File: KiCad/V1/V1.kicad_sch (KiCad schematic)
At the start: 84 parts, among them Q1 Q_NMOS_GSD, Q2 Q_NMOS_GSD, T1 Transformer_1P_1S, U1 LMG1210RVRR, U2 OPA2677IDDA, U3 OPA2677IDDA, U4 OPA859QDSGRQ1, U5 OPA859QDSGRQ1, U6 OPA859QDSGRQ1

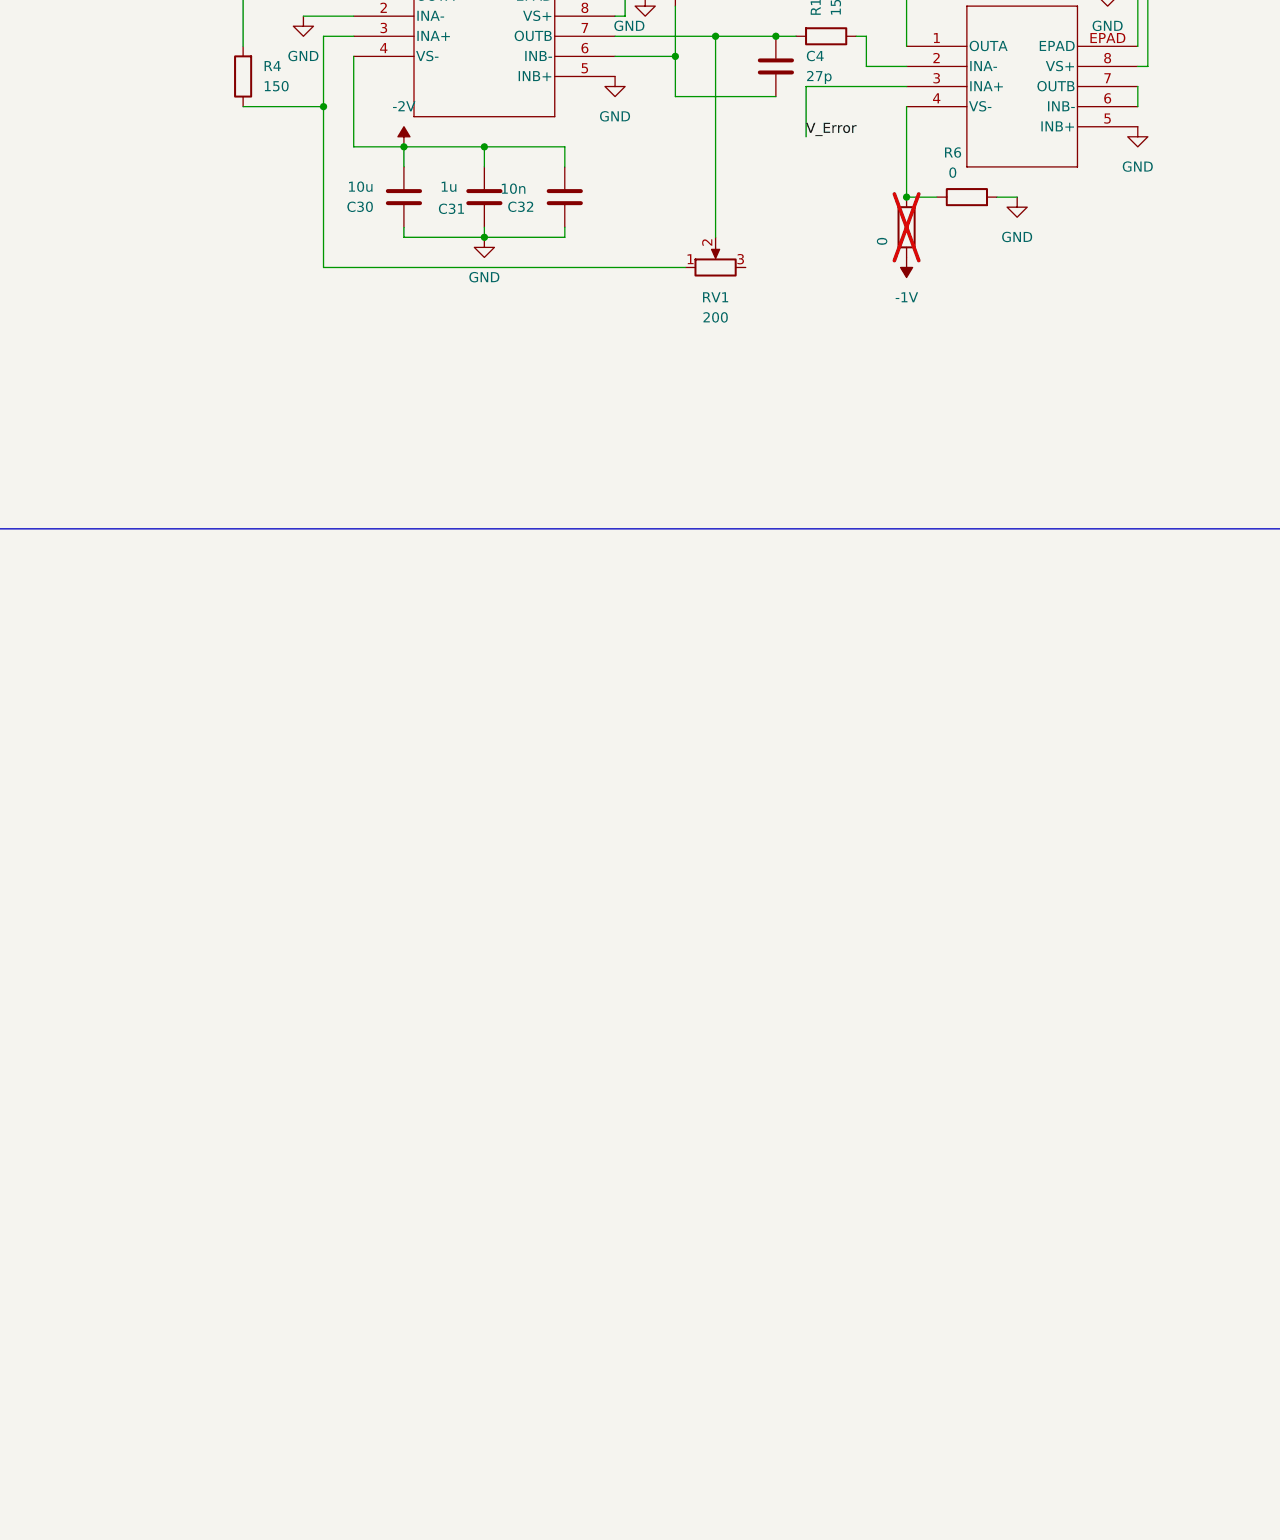
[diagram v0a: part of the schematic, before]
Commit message: fixed pwm gen negative supply voltage
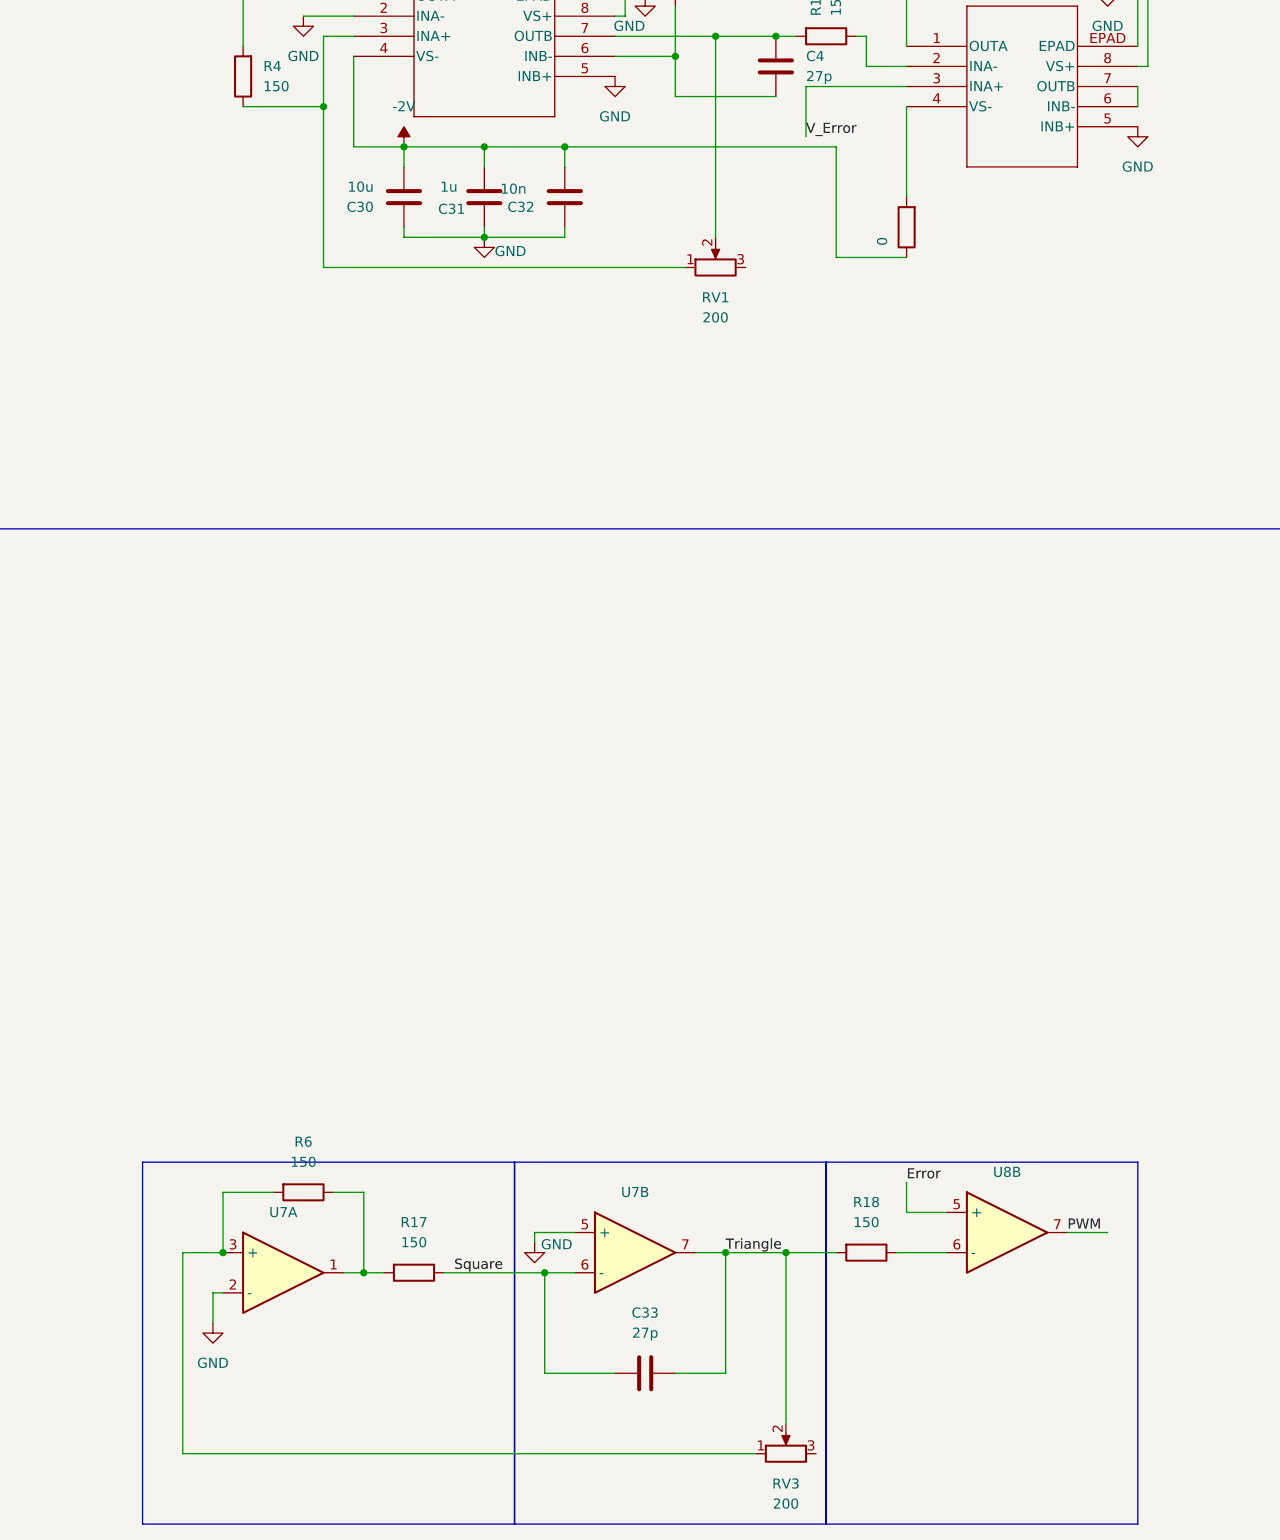
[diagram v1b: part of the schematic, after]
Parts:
- added C33: 27p, Capacitor_SMD:C_0402_1005Metric, symbol Device:C
- added R17, R18: 150, symbol Device:R
- added RV3: 200, MyFootprints:POT_ 3214W-1-201E, symbol Device:R_Potentiometer
- added U7: OPAMP, symbol Device:Opamp_Dual
- added U8: Compariotr, symbol Device:Opamp_Dual
- R3: now fitted
- R6: value 0 -> 150; footprint Capacitor_SMD:C_0805_2012Metric -> (none)
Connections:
- net -1V is gone; now on net -2V: R3.1
- net GND: now also U7.2 (-), U7.5 (+); no longer R6.2
- net at R3.2, U3.4 (VS-): no longer R6.1
- new net: R17.2, R6.1, U7.1
- new net: R6.2, RV3.1, U7.3 (+)
- new net: R18.1, U8.6 (-)
- new net Error: U8.5 (+)
- new net PWM: U8.7
- new net Square: C33.1, R17.1, U7.6 (-)
- new net Triangle: C33.2, R18.2, RV3.2, U7.7

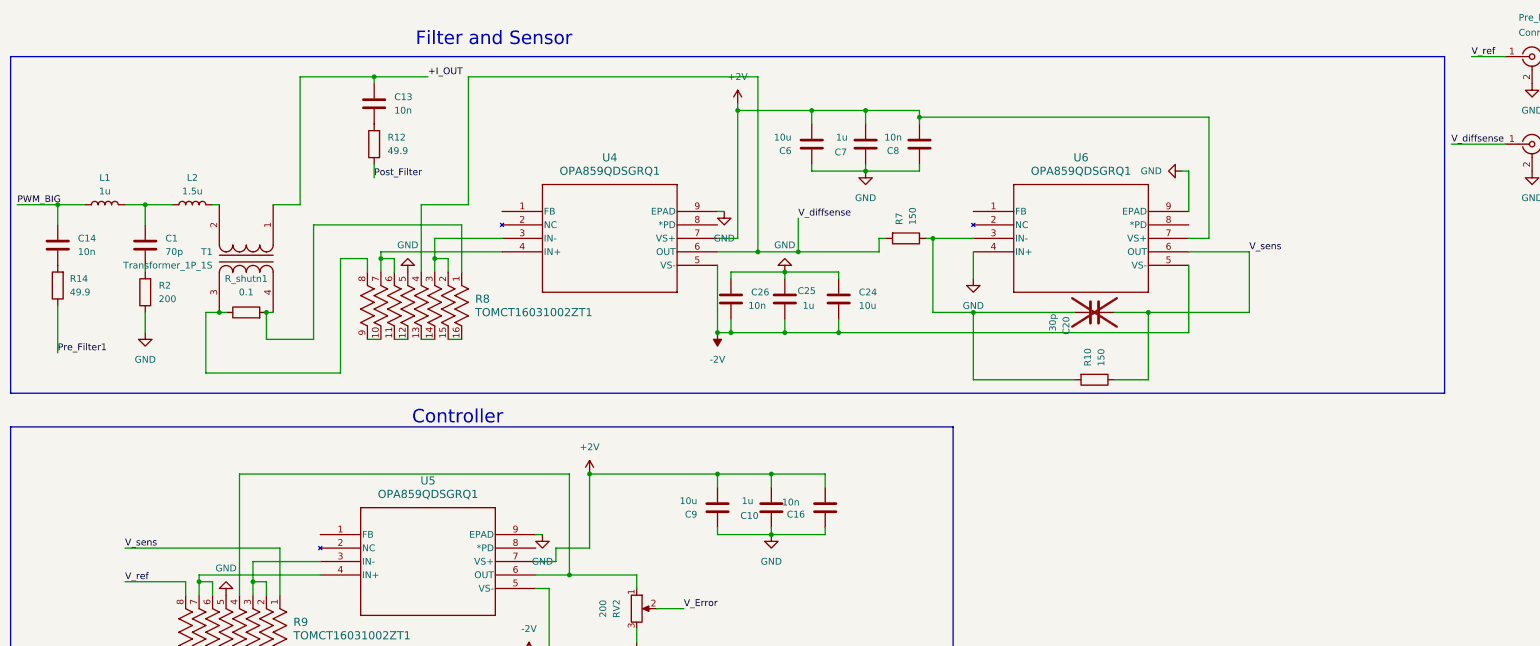
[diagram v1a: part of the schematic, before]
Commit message: aded alternative path for curent sense signal
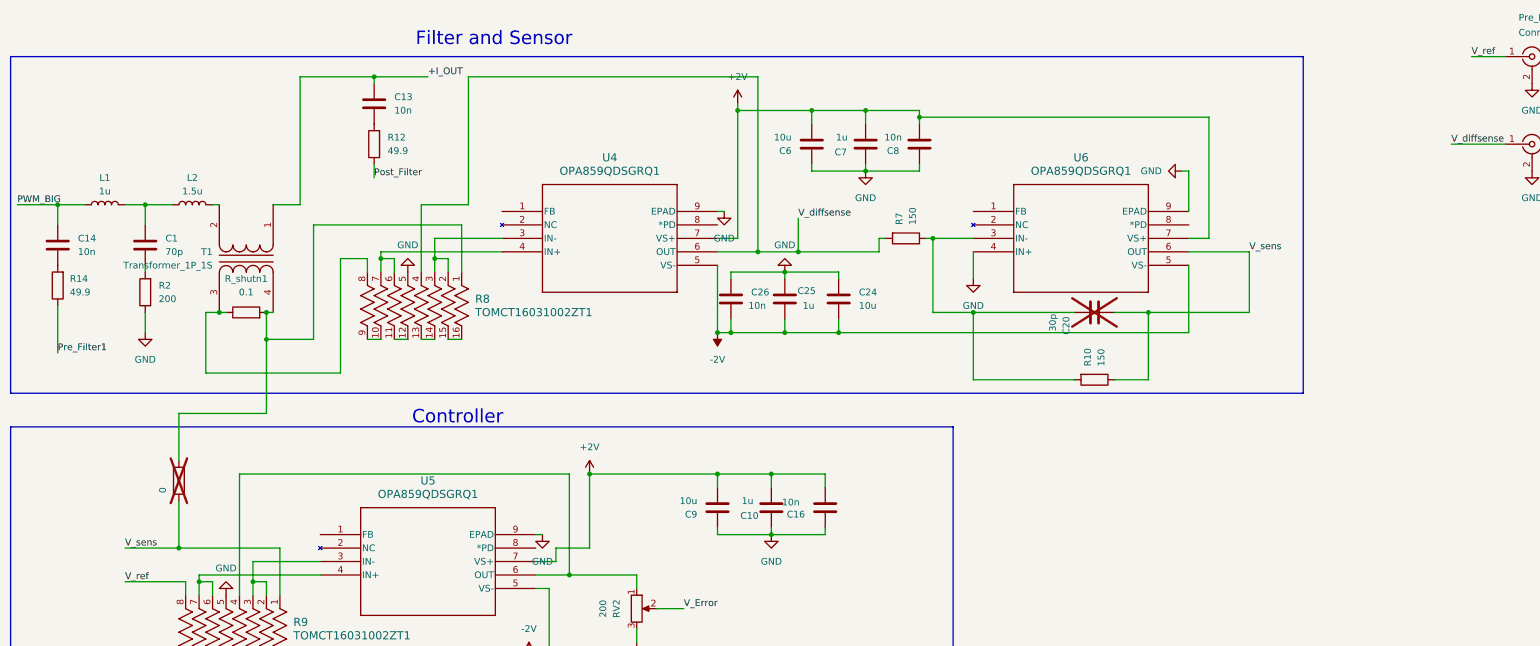
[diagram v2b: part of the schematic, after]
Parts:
- added R19: 0, Capacitor_SMD:C_0805_2012Metric, symbol Device:R
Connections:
- net V_sens: now also R19.1
- net at R8.1, R_shutn1.2, T1.4 (SB): now also R19.2
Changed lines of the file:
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@@
 	)
 	(junction
+		(at 54.61 115.57)
+		(diameter 0)
+		(color 0 0 0 0)
+	)
+	(junction
 		(at 95.25 217.17)
 		(diameter 0)
@@
 	)
 	(junction
+		(at 71.12 76.2)
+		(diameter 0)
+		(color 0 0 0 0)
+	)
+	(junction
 		(at 156.21 74.93)
 		(diameter 0)
@@
 	(wire
 		(pts
-			(xy 44.45 115.57) (xy 73.66 115.57)
+			(xy 44.45 115.57) (xy 54.61 115.57)
 		)
 		(stroke
@@
 	(wire
 		(pts
+			(xy 54.61 90.17) (xy 71.12 90.17)
+		)
+		(stroke
+			(width 0)
+			(type default)
+		)
+	)
+	(wire
+		(pts
 			(xy 74.93 217.17) (xy 85.09 217.17)
 		)
@@
 	(wire
 		(pts
+			(xy 54.61 99.06) (xy 54.61 90.17)
+		)
+		(stroke
+			(width 0)
+			(type default)
+		)
+	)
+	(wire
+		(pts
 			(xy 48.26 71.12) (xy 48.26 74.93)
 		)
@@
 	(wire
 		(pts
+			(xy 71.12 90.17) (xy 71.12 76.2)
+		)
+		(stroke
+			(width 0)
+			(type default)
+		)
+	)
+	(wire
+		(pts
 			(xy 311.15 175.26) (xy 320.04 175.26)
 		)
@@
 	(wire
 		(pts
+			(xy 54.61 106.68) (xy 54.61 115.57)
+		)
+		(stroke
+			(width 0)
+			(type default)
+		)
+	)
+	(wire
+		(pts
 			(xy 138.43 189.23) (xy 140.97 189.23)
 		)
@@
 	(wire
 		(pts
+			(xy 54.61 115.57) (xy 73.66 115.57)
+		)
+		(stroke
+			(width 0)
+			(type default)
+		)
+	)
+	(wire
+		(pts
 			(xy 68.58 191.77) (xy 68.58 198.12)
 		)
@@
 	(rectangle
 		(start 22.86 22.86)
-		(end 293.37 86.36)
+		(end 266.7 86.36)
 		(stroke
 			(width 0)
@@
 					(unit 1)
 				)
+			)
+		)
+	)
+	(symbol
+		(lib_id "Device:R")
+		(at 54.61 102.87 180)
+		(unit 1)
+		(exclude_from_sim no)
+		(in_bom yes)
+		(on_board yes)
+		(dnp yes)
+		(property "Reference" "R19"
+			(at 49.022 104.648 90)
+			(effects
+				(font
+					(size 1.27 1.27)
+				)
+				(hide yes)
+			)
+		)
+		(property "Value" "0"
+			(at 51.562 104.648 90)
+			(effects
+				(font
+					(size 1.27 1.27)
+				)
+			)
+		)
+		(property "Footprint" "Capacitor_SMD:C_0805_2012Metric"
+			(at 56.388 102.87 90)
+			(effects
+				(font
+					(size 1.27 1.27)
+				)
+				(hide yes)
+			)
+		)
+		(property "Datasheet" "~"
+			(at 54.61 102.87 0)
+			(effects
+				(font
+					(size 1.27 1.27)
+				)
+				(hide yes)
+			)
+		)
+		(property "Description" "Resistor"
+			(at 54.61 102.87 0)
+			(effects
+				(font
+					(size 1.27 1.27)
+				)
+				(hide yes)
+			)
+		)
+		(pin "1"
+		)
+		(pin "2"
+		)
+		(instances
+			(project "V1"
+				(path "/009e4554-048b-4d13-979d-7fdd312db04d"
+					(reference "R19")
+					(unit 1)
+				)

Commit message: ccdesign matlab
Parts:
- removed R19: 0, Capacitor_SMD:C_0805_2012Metric, symbol Device:R
- R8, R9: value TOMCT16031002ZT1 -> NOMCT16
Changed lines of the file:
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@@
 	)
 	(junction
-		(at 54.61 115.57)
-		(diameter 0)
-		(color 0 0 0 0)
-	)
-	(junction
 		(at 95.25 217.17)
 		(diameter 0)
@@
 	)
 	(junction
-		(at 71.12 76.2)
-		(diameter 0)
-		(color 0 0 0 0)
-	)
-	(junction
 		(at 156.21 74.93)
 		(diameter 0)
@@
 	(wire
 		(pts
-			(xy 44.45 115.57) (xy 54.61 115.57)
-		)
-		(stroke
-			(width 0)
-			(type default)
-		)
-	)
-	(wire
-		(pts
 			(xy 77.47 26.67) (xy 77.47 50.8)
 		)
@@
 	(wire
 		(pts
-			(xy 54.61 90.17) (xy 71.12 90.17)
-		)
-		(stroke
-			(width 0)
-			(type default)
-		)
-	)
-	(wire
-		(pts
 			(xy 74.93 217.17) (xy 85.09 217.17)
 		)
@@
 	(wire
 		(pts
-			(xy 54.61 99.06) (xy 54.61 90.17)
-		)
-		(stroke
-			(width 0)
-			(type default)
-		)
-	)
-	(wire
-		(pts
 			(xy 48.26 71.12) (xy 48.26 74.93)
 		)
@@
 	(wire
 		(pts
-			(xy 71.12 90.17) (xy 71.12 76.2)
-		)
-		(stroke
-			(width 0)
-			(type default)
-		)
-	)
-	(wire
-		(pts
 			(xy 311.15 175.26) (xy 320.04 175.26)
 		)
@@
 	(wire
 		(pts
-			(xy 54.61 106.68) (xy 54.61 115.57)
-		)
-		(stroke
-			(width 0)
-			(type default)
-		)
-	)
-	(wire
-		(pts
 			(xy 138.43 189.23) (xy 140.97 189.23)
 		)
@@
 	(wire
 		(pts
-			(xy 54.61 115.57) (xy 73.66 115.57)
+			(xy 44.45 115.57) (xy 73.66 115.57)
 		)
 		(stroke
@@
 	(symbol
 		(lib_id "Device:R")
-		(at 54.61 102.87 180)
-		(unit 1)
-		(exclude_from_sim no)
-		(in_bom yes)
-		(on_board yes)
-		(dnp yes)
-		(property "Reference" "R19"
-			(at 49.022 104.648 90)
-			(effects
-				(font
-					(size 1.27 1.27)
-				)
-				(hide yes)
-			)
-		)
-		(property "Value" "0"
-			(at 51.562 104.648 90)
-			(effects
-				(font
-					(size 1.27 1.27)
-				)
-			)
-		)
-		(property "Footprint" "Capacitor_SMD:C_0805_2012Metric"
-			(at 56.388 102.87 90)
-			(effects
-				(font
-					(size 1.27 1.27)
-				)
-				(hide yes)
-			)
-		)
-		(property "Datasheet" "~"
-			(at 54.61 102.87 0)
-			(effects
-				(font
-					(size 1.27 1.27)
-				)
-				(hide yes)
-			)
-		)
-		(property "Description" "Resistor"
-			(at 54.61 102.87 0)
-			(effects
-				(font
-					(size 1.27 1.27)
-				)
-				(hide yes)
-			)
-		)
-		(pin "1"
-		)
-		(pin "2"
-		)
-		(instances
-			(project "V1"
-				(path "/009e4554-048b-4d13-979d-7fdd312db04d"
-					(reference "R19")
-					(unit 1)
-				)
-			)
-		)
-	)
-	(symbol
-		(lib_id "Device:R")
 		(at 242.57 195.58 90)
 		(unit 1)
@@
 			)
 		)
-		(property "Value" "TOMCT16031002ZT1"
+		(property "Value" "NOMCT16"
 			(at 110.49 71.1199 90)
 			(effects
@@
 			)
 		)
-		(property "Value" "TOMCT16031002ZT1"
+		(property "Value" "NOMCT16"
 			(at 76.2 132.0799 90)
 			(effects
